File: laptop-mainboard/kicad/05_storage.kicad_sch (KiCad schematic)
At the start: 5 parts, among them U21 SY6280_LoadSW, U22 SY6280_LoadSW

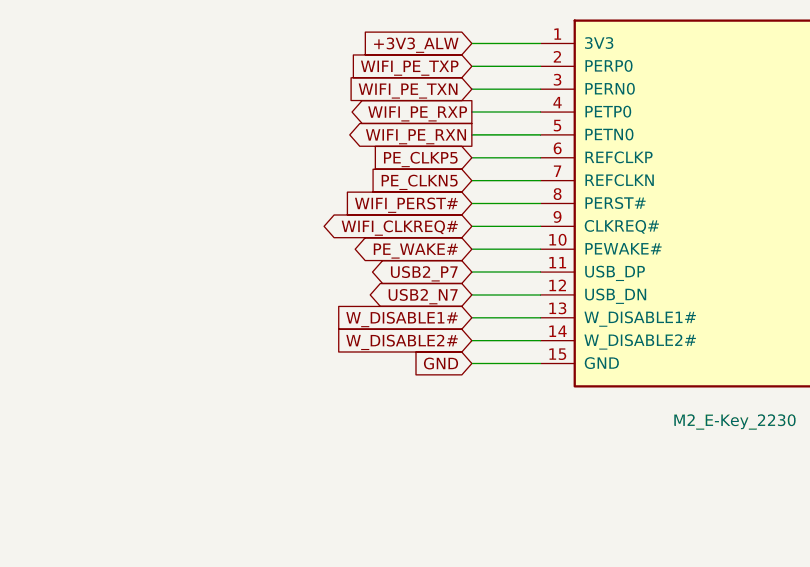
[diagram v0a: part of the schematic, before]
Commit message: Rev B: echte AM5-Pinbelegung, Kleinteile, EliteBook-850-G7-Format
- AM5-Pinmap (1718 Pins, WikiChip/Wikimedia Public Domain) als CSV,
  Sockel-Footprint mit echten Padnamen und 1708 Signal-Netzen im Board
- Blatt 10: MLCC-Baenke, 11 ESD-Arrays, USB2-Chokes, Straps; 48-MHz-Quarz;
  beidseitige Bestueckung (B.Cu) mit Kollisionspruefung pro Seite
- Board 340x112mm im EliteBook-850-G7-Layout: USB-C-100W-PD an der
  Barrel-Jack-Position, TB4/HDMI/USB-A/RJ45 rechts, USB-A/Klinke links,
  HP-Akku 3S/56Wh, HP-FPC-Steckplaetze (Pinouts zu verifizieren)
- GND-Stitching-Vias, MDI-/DP-Korridore, 645 Board-Netze
- Renderer tools/render_board.py erzeugt docs/board_render.png
- Doku: elitebook.md neu, grenzen.md/README/power/layout aktualisiert

Co-Authored-By: Claude Fable 5 <noreply@anthropic.com>
Claude-Session: https://claude.ai/code/session_01E8mU1RUAv938Hs69waADCc
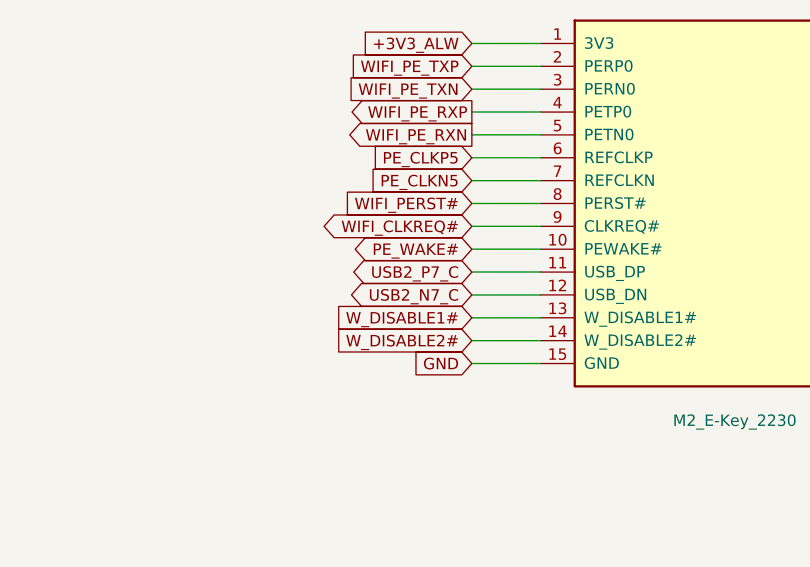
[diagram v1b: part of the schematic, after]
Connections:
- net USB2_N7 renamed USB2_N7_C
- net USB2_P7 renamed USB2_P7_C
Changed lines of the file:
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@@
     (pin "11")
     (pin "12")
-    (instances (project "laptop-mainboard" (path "/d22f2c28-8e23-5b8e-ba77-63ae2c13187c/0f5f316f-94d7-5320-855f-bd2242f4c4d2" (reference "J_SSD1") (unit 1))))
+    (instances (project "laptop-mainboard" (path "/d22f2c28-8e23-5b8e-ba77-63ae2c13187c/64471f9c-6c32-59f2-bbf0-9ae71c886002" (reference "J_SSD1") (unit 1))))
   )
   (wire (pts (xy 118.41 46.99) (xy 110.79 46.99)) (stroke (width 0) (type default)))
@@
     (pin "3")
     (pin "4")
-    (instances (project "laptop-mainboard" (path "/d22f2c28-8e23-5b8e-ba77-63ae2c13187c/0f5f316f-94d7-5320-855f-bd2242f4c4d2" (reference "U21") (unit 1))))
+    (instances (project "laptop-mainboard" (path "/d22f2c28-8e23-5b8e-ba77-63ae2c13187c/64471f9c-6c32-59f2-bbf0-9ae71c886002" (reference "U21") (unit 1))))
   )
   (wire (pts (xy 126.03 97.79) (xy 118.41 97.79)) (stroke (width 0) (type default)))
@@
     (pin "11")
     (pin "12")
-    (instances (project "laptop-mainboard" (path "/d22f2c28-8e23-5b8e-ba77-63ae2c13187c/0f5f316f-94d7-5320-855f-bd2242f4c4d2" (reference "J_SSD2") (unit 1))))
+    (instances (project "laptop-mainboard" (path "/d22f2c28-8e23-5b8e-ba77-63ae2c13187c/64471f9c-6c32-59f2-bbf0-9ae71c886002" (reference "J_SSD2") (unit 1))))
   )
   (wire (pts (xy 308.41 46.99) (xy 300.79 46.99)) (stroke (width 0) (type default)))
@@
     (pin "3")
     (pin "4")
-    (instances (project "laptop-mainboard" (path "/d22f2c28-8e23-5b8e-ba77-63ae2c13187c/0f5f316f-94d7-5320-855f-bd2242f4c4d2" (reference "U22") (unit 1))))
+    (instances (project "laptop-mainboard" (path "/d22f2c28-8e23-5b8e-ba77-63ae2c13187c/64471f9c-6c32-59f2-bbf0-9ae71c886002" (reference "U22") (unit 1))))
   )
   (wire (pts (xy 316.03 97.79) (xy 308.41 97.79)) (stroke (width 0) (type default)))
@@
     (pin "14")
     (pin "15")
-    (instances (project "laptop-mainboard" (path "/d22f2c28-8e23-5b8e-ba77-63ae2c13187c/0f5f316f-94d7-5320-855f-bd2242f4c4d2" (reference "J_WIFI") (unit 1))))
+    (instances (project "laptop-mainboard" (path "/d22f2c28-8e23-5b8e-ba77-63ae2c13187c/64471f9c-6c32-59f2-bbf0-9ae71c886002" (reference "J_WIFI") (unit 1))))
   )
   (wire (pts (xy 478.41 46.99) (xy 470.79 46.99)) (stroke (width 0) (type default)))
@@
   )
   (wire (pts (xy 478.41 72.39) (xy 470.79 72.39)) (stroke (width 0) (type default)))
-  (global_label "USB2_P7" (shape bidirectional) (at 470.79 72.39 180) (fields_autoplaced yes)
+  (global_label "USB2_P7_C" (shape bidirectional) (at 470.79 72.39 180) (fields_autoplaced yes)
     (effects (font (size 1.27 1.27)) (justify right))
     (property "Intersheetrefs" "${INTERSHEET_REFS}" (at 470.79 72.39 0) (effects (font (size 1.27 1.27)) (hide yes)))
   )
   (wire (pts (xy 478.41 74.93) (xy 470.79 74.93)) (stroke (width 0) (type default)))
-  (global_label "USB2_N7" (shape bidirectional) (at 470.79 74.93 180) (fields_autoplaced yes)
+  (global_label "USB2_N7_C" (shape bidirectional) (at 470.79 74.93 180) (fields_autoplaced yes)
     (effects (font (size 1.27 1.27)) (justify right))
     (property "Intersheetrefs" "${INTERSHEET_REFS}" (at 470.79 74.93 0) (effects (font (size 1.27 1.27)) (hide yes)))
